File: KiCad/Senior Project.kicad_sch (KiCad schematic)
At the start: 30 parts, among them J1 USB_C_Receptacle_USB2.0_16P, J2 Screw_Terminal_01x02, J3 Screw_Terminal_01x06, SW1 SW_Push, SW2 SW_Push, U1 ESP32-S3FH4R2, X1 FC-135 32.7680KA-A5, Y2 Crystal_GND23

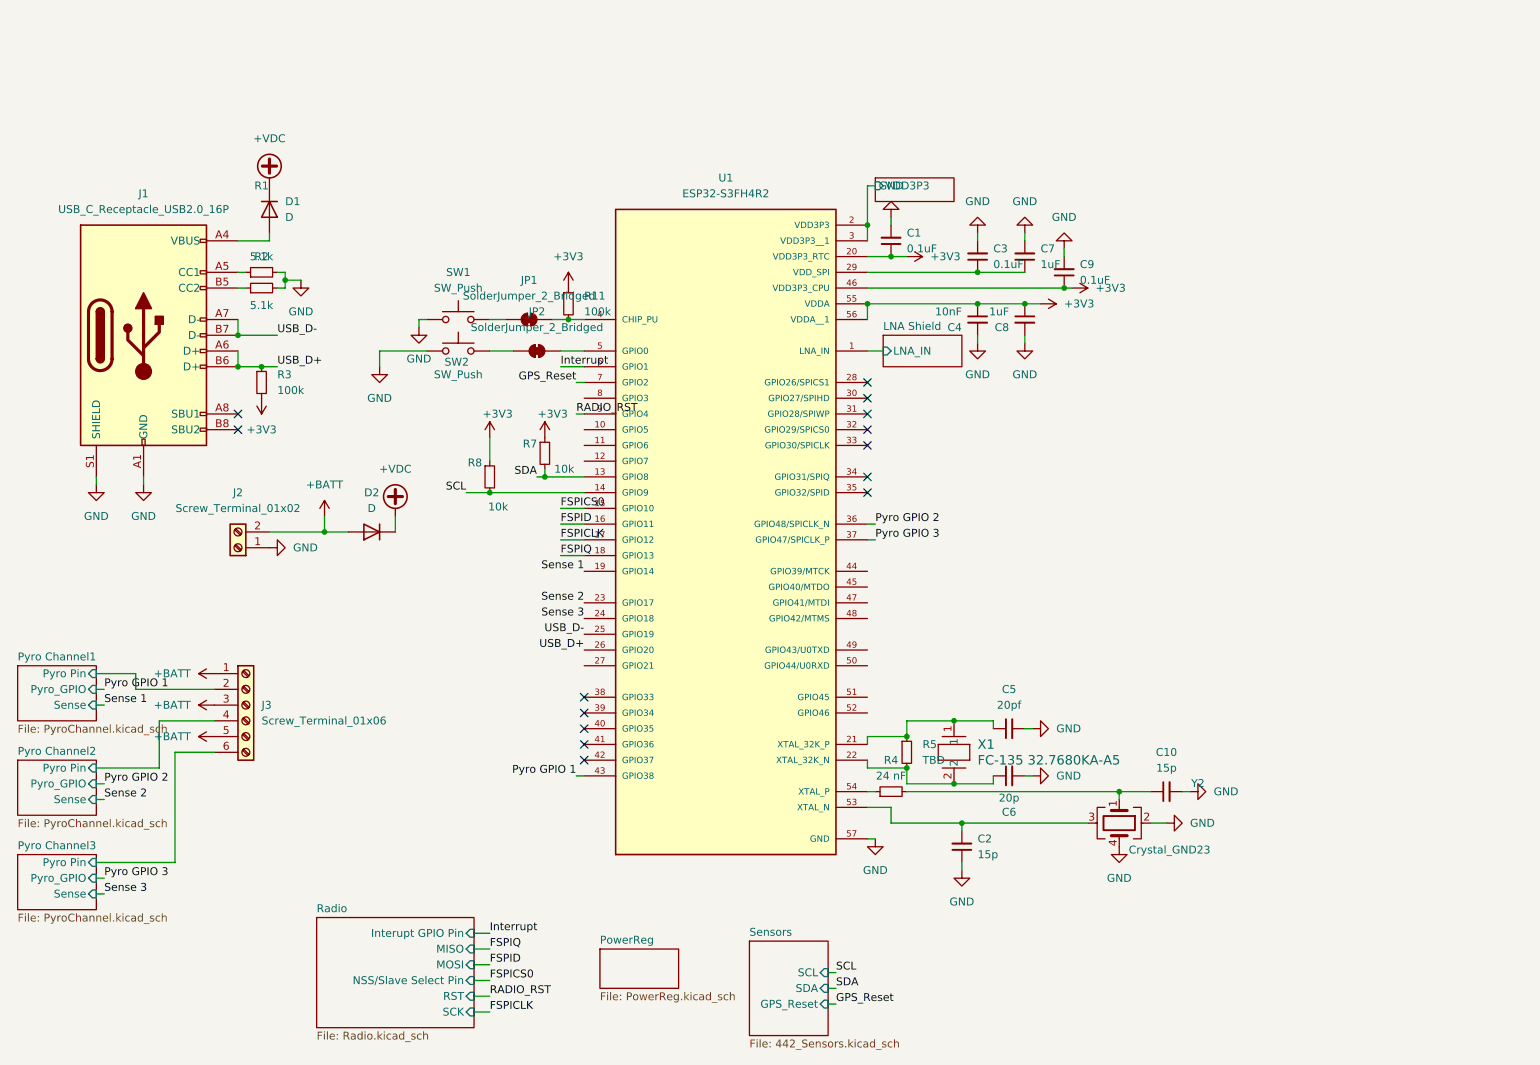
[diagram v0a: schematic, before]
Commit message: Removed micrcontroller
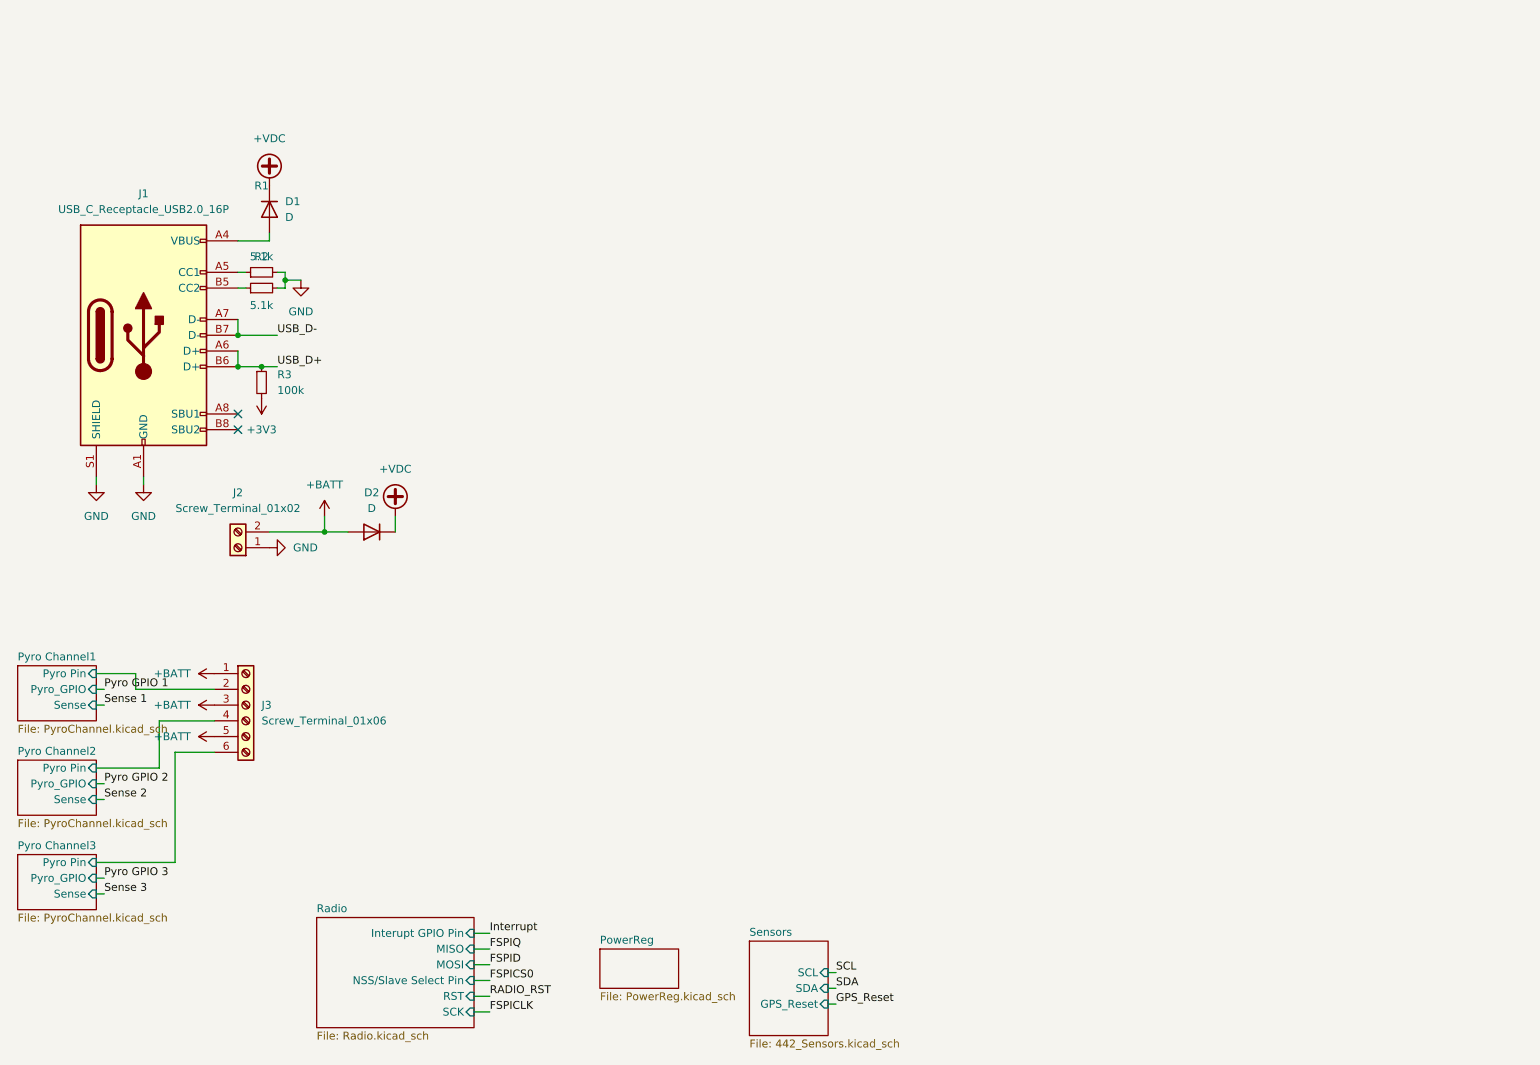
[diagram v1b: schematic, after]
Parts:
- removed C1, C3, C9: 0.1uF, Capacitor_SMD:C_0402_1005Metric, symbol Device:C_Small
- removed C10, C2: 15p, Capacitor_SMD:C_0402_1005Metric, symbol Device:C_Small
- removed C4: 10nF, Capacitor_SMD:C_0402_1005Metric, symbol Device:C_Small
- removed C5: 20pf, Capacitor_SMD:C_0402_1005Metric, symbol Device:C_Small
- removed C6: 20p, Capacitor_SMD:C_0402_1005Metric, symbol Device:C_Small
- removed C7, C8: 1uF, Capacitor_SMD:C_0402_1005Metric, symbol Device:C_Small
- removed JP1, JP2: SolderJumper_2_Bridged, Jumper:SolderJumper-2_P1.3mm_Bridged_RoundedPad1.0x1.5mm, symbol Jumper:SolderJumper_2_Bridged
- removed R11: 100k, Resistor_SMD:R_0402_1005Metric, symbol Device:R_Small
- removed R4: 24 nF, Capacitor_SMD:C_0402_1005Metric, symbol Device:R_Small
- removed R5: TBD, Capacitor_SMD:C_0402_1005Metric, symbol Device:R_Small
- removed R7, R8: 10k, Resistor_SMD:R_0402_1005Metric, symbol Device:R_Small
- removed SW1, SW2: SW_Push, Button_Switch_SMD:SW_SPST_PTS810, symbol Switch:SW_Push
- removed U1: ESP32-S3FH4R2, S3FH4R2:QFN40P700X700X90-57N, symbol ESP32-S3FH4R2:ESP32-S3FH4R2
- removed X1: FC-135 32.7680KA-A5, FC-135:XTAL_FC-135_EPS, symbol FC_135:FC-135_32.7680KA-A5
- removed Y2: Crystal_GND23, Crystal:Crystal_SMD_3225-4Pin_3.2x2.5mm, symbol Device:Crystal_GND23
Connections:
- no-connect marks 14 -> 2
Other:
- removed sheet ESP-32 Power Coupler
- removed sheet LNA Shield

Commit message: Added some basic pin outs
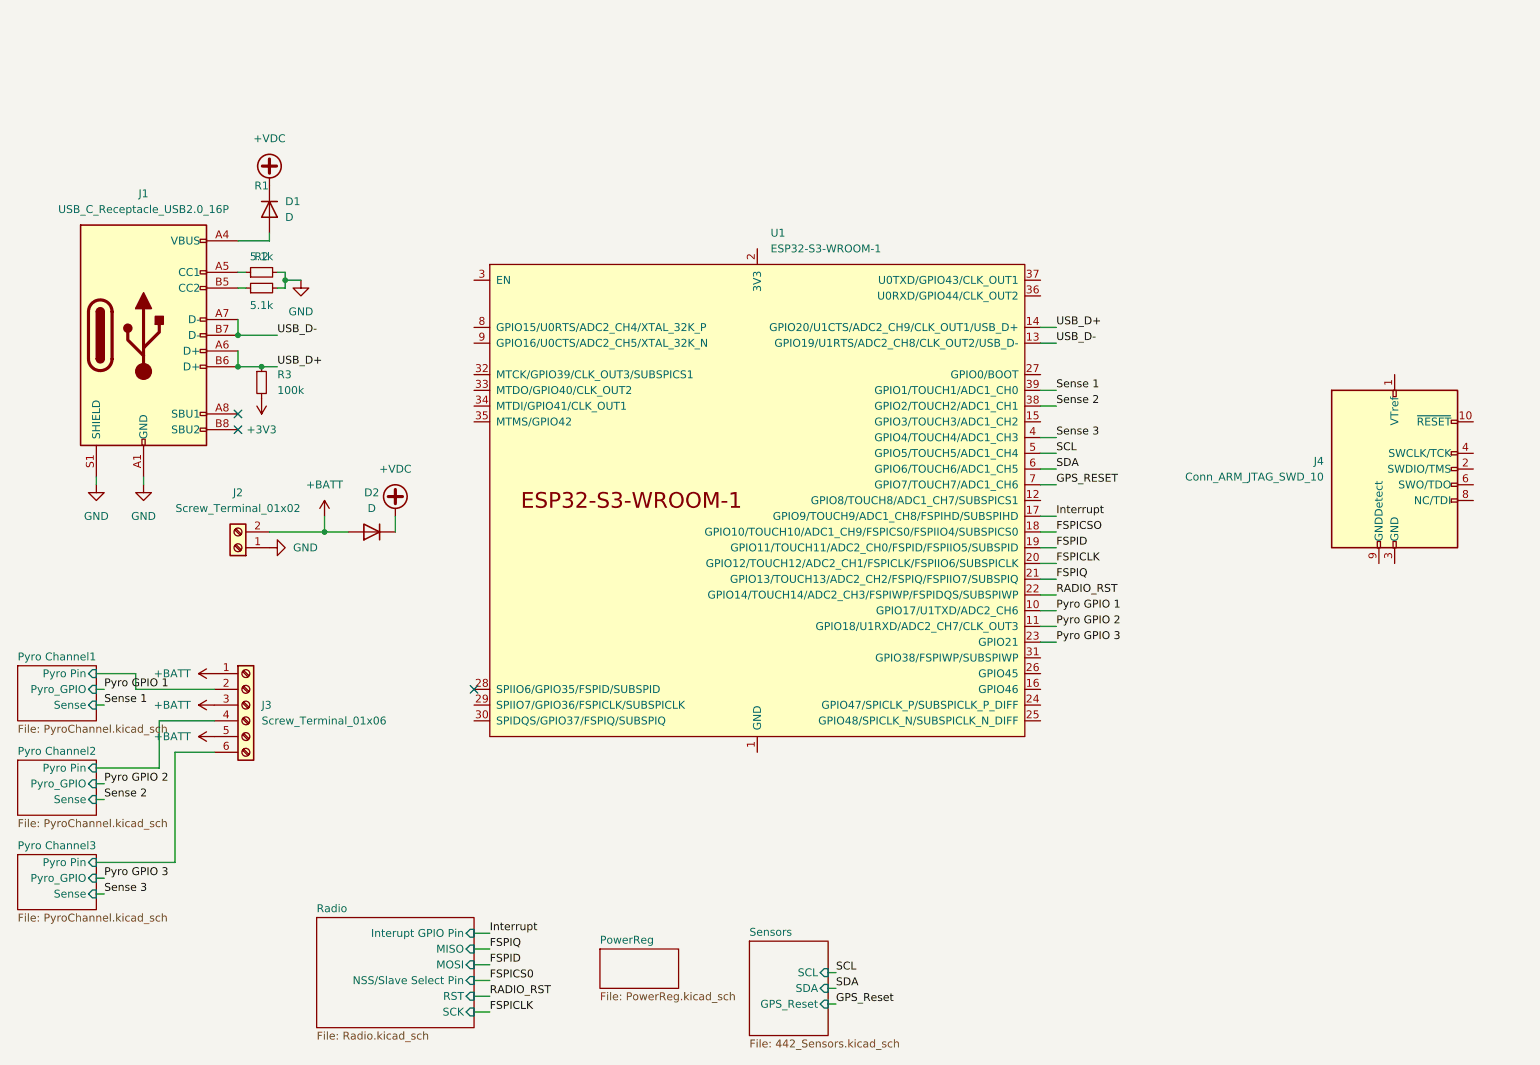
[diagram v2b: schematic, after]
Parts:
- added J4: Conn_ARM_JTAG_SWD_10, symbol Connector:Conn_ARM_JTAG_SWD_10
- added U1: ESP32-S3-WROOM-1, PCM_Espressif:ESP32-S3-WROOM-1, symbol Espressif:ESP32-S3-WROOM-1
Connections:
- net FSPICLK: now also U1.20 (GPIO12/TOUCH12/ADC2_CH1/FSPICLK/FSPIIO6/SUBSPICLK)
- net FSPID: now also U1.19 (GPIO11/TOUCH11/ADC2_CH0/FSPID/FSPIIO5/SUBSPID)
- net FSPIQ: now also U1.21 (GPIO13/TOUCH13/ADC2_CH2/FSPIQ/FSPIIO7/SUBSPIQ)
- net Interrupt: now also U1.17 (GPIO9/TOUCH9/ADC1_CH8/FSPIHD/SUBSPIHD)
- net Pyro GPIO 1: now also U1.10 (GPIO17/U1TXD/ADC2_CH6)
- net Pyro GPIO 2: now also U1.11 (GPIO18/U1RXD/ADC2_CH7/CLK_OUT3)
- net Pyro GPIO 3: now also U1.23 (GPIO21)
- net RADIO_RST: now also U1.22 (GPIO14/TOUCH14/ADC2_CH3/FSPIWP/FSPIDQS/SUBSPIWP)
- net SCL: now also U1.5 (GPIO5/TOUCH5/ADC1_CH4)
- net SDA: now also U1.6 (GPIO6/TOUCH6/ADC1_CH5)
- net Sense 1: now also U1.39 (GPIO1/TOUCH1/ADC1_CH0)
- net Sense 2: now also U1.38 (GPIO2/TOUCH2/ADC1_CH1)
- net Sense 3: now also U1.4 (GPIO4/TOUCH4/ADC1_CH3)
- net USB_D+: now also U1.14 (GPIO20/U1CTS/ADC2_CH9/CLK_OUT1/USB_D+)
- net USB_D-: now also U1.13 (GPIO19/U1RTS/ADC2_CH8/CLK_OUT2/USB_D-)
- new net: J4.3 (GND), J4.5 (GND)
- new net: U1.1 (GND), U1.40 (GND), U1.41 (GND)
- new net FSPICSO: U1.18 (GPIO10/TOUCH10/ADC1_CH9/FSPICS0/FSPIIO4/SUBSPICS0)
- new net GPS_RESET: U1.7 (GPIO7/TOUCH7/ADC1_CH6)
- no-connect marks 2 -> 3

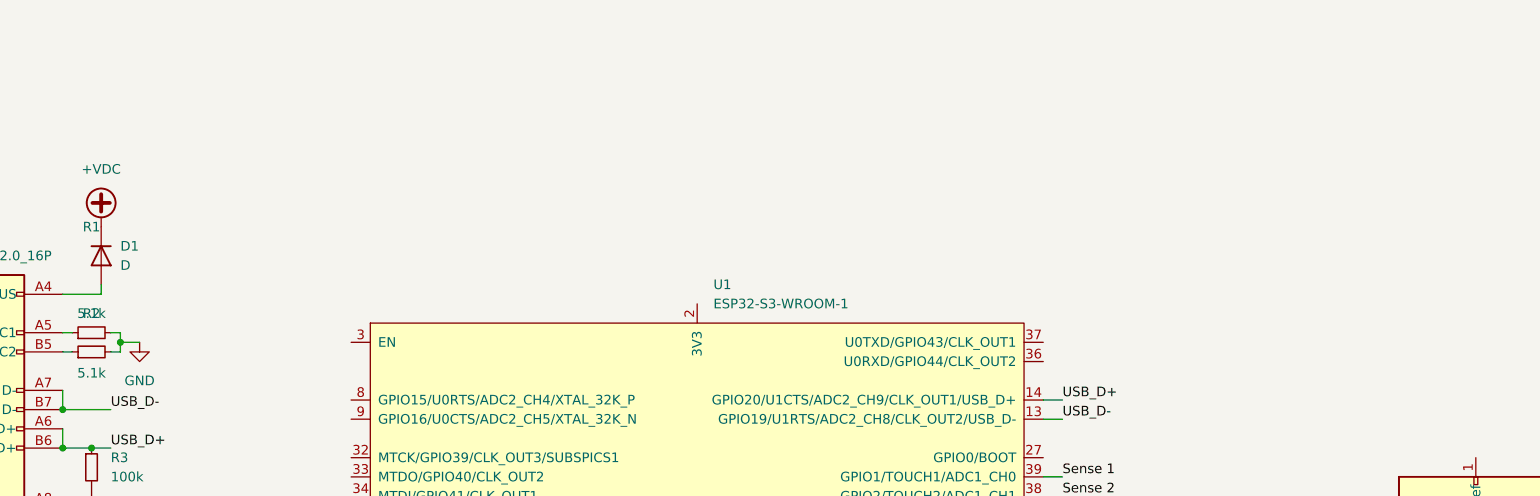
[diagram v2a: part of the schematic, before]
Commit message: Added pushbuttons and power coupling
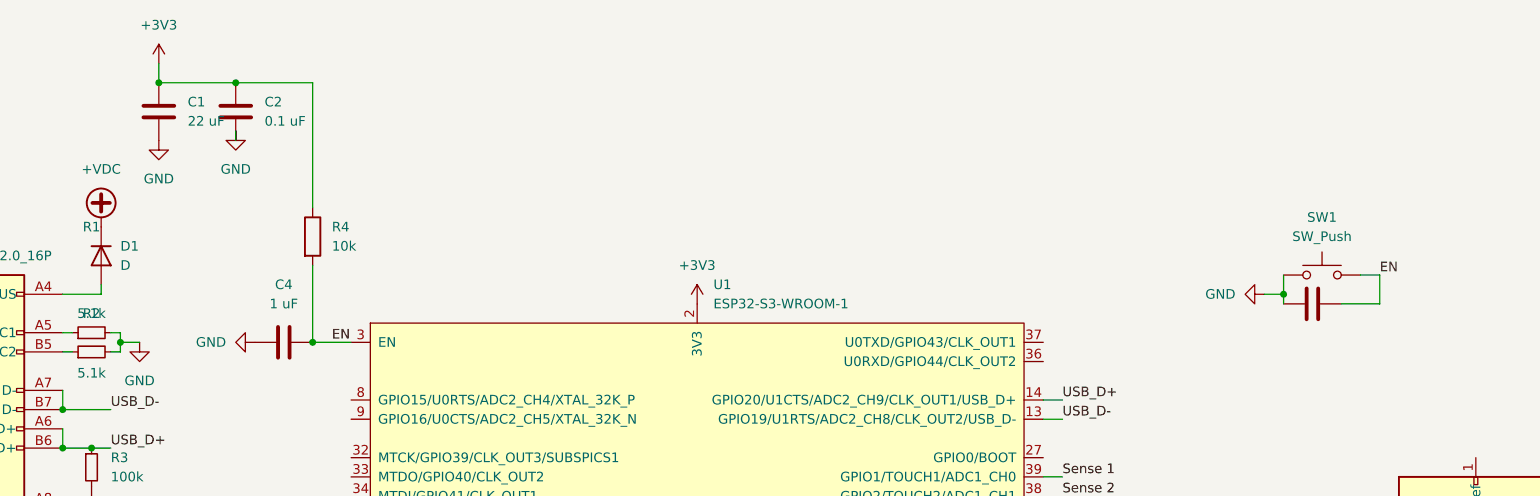
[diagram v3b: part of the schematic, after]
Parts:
- added C1: 22 uF, symbol Device:C
- added C2, C3: 0.1 uF, symbol Device:C
- added C4: 1 uF, symbol Device:C
- added R4: 10k, symbol Device:R
- added SW1: SW_Push, symbol Switch:SW_Push
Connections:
- net +3V3: now also U1.2 (3V3), C1.1, C2.1, R4.1
- net GND: now also C1.2, C2.2, C3.1, C4.1, SW1.1
- net EN: now reaches U1.3 (EN)
- net EN: now also C3.2, C4.2, R4.2, SW1.2

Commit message: Added jtag interface
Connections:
- net +3V3: now also J4.1 (VTref)
- net GND: now also J4.3 (GND), J4.5 (GND)
- net MTMS: now reaches J4.2 (SWDIO/TMS)
- net MTMS: now also U1.35 (MTMS/GPIO42)
- net MTCK: now reaches J4.4 (SWCLK/TCK)
- net MTCK: now also U1.32 (MTCK/GPIO39/CLK_OUT3/SUBSPICS1)
- net MTD0: now reaches J4.6 (SWO/TDO)
- net MTDI: now reaches J4.8 (NC/TDI)
- net MTDI: now also U1.34 (MTDI/GPIO41/CLK_OUT1)
- net MTDO: now reaches U1.33 (MTDO/GPIO40/CLK_OUT2)
